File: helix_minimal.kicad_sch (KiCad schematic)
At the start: 15 parts, among them J1 USB-C, J2 WIZ850io J1, J3 WIZ850io J2, J4 3V3 microSD SPI breakout, J5 SWD, U1 STM32C071FBP6, U2 AP2112K-3.3

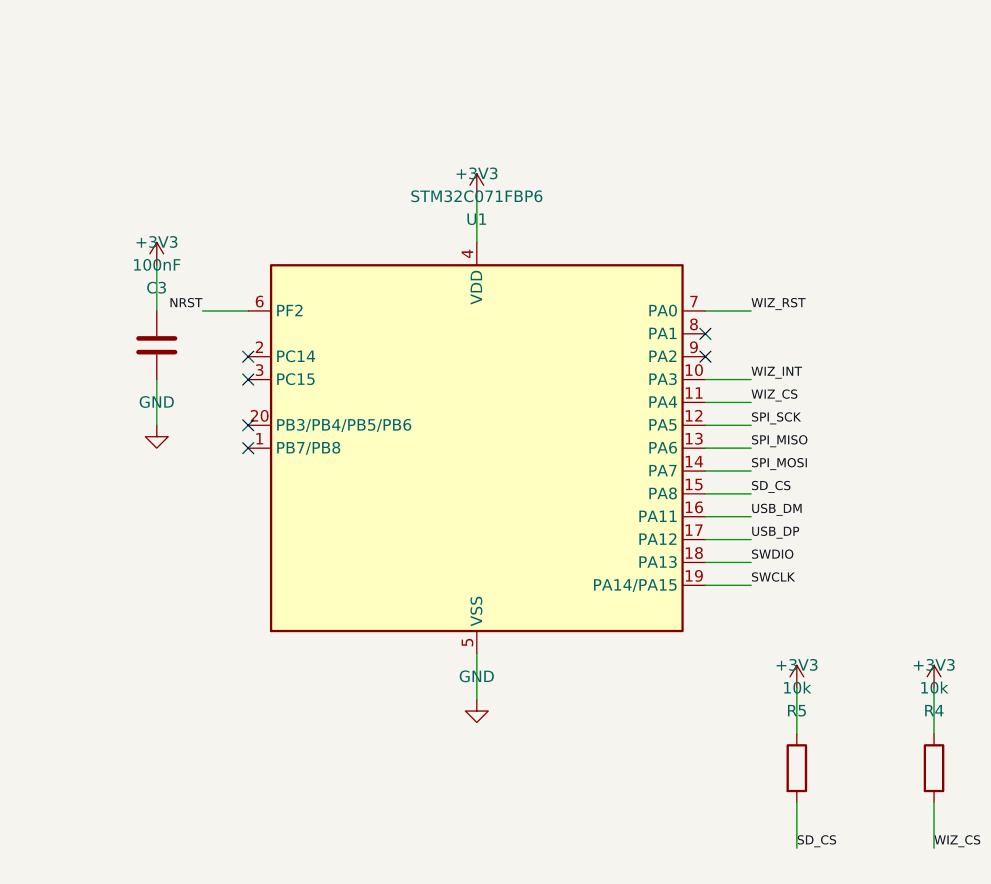
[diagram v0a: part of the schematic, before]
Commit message: Align STM32 connections with edited symbol
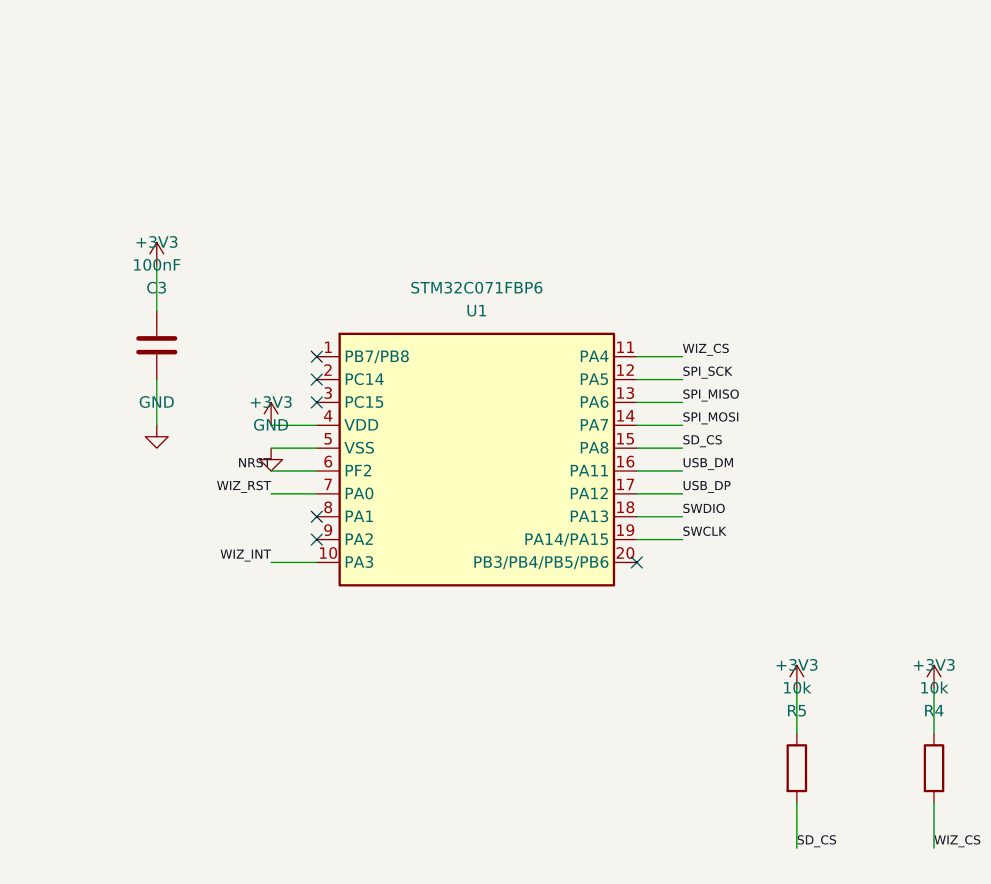
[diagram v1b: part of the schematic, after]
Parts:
- U1: symbol MCU_ST_STM32C0:STM32C071FBPx -> Helix:STM32C071FBPx
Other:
- moved on the sheet: U1

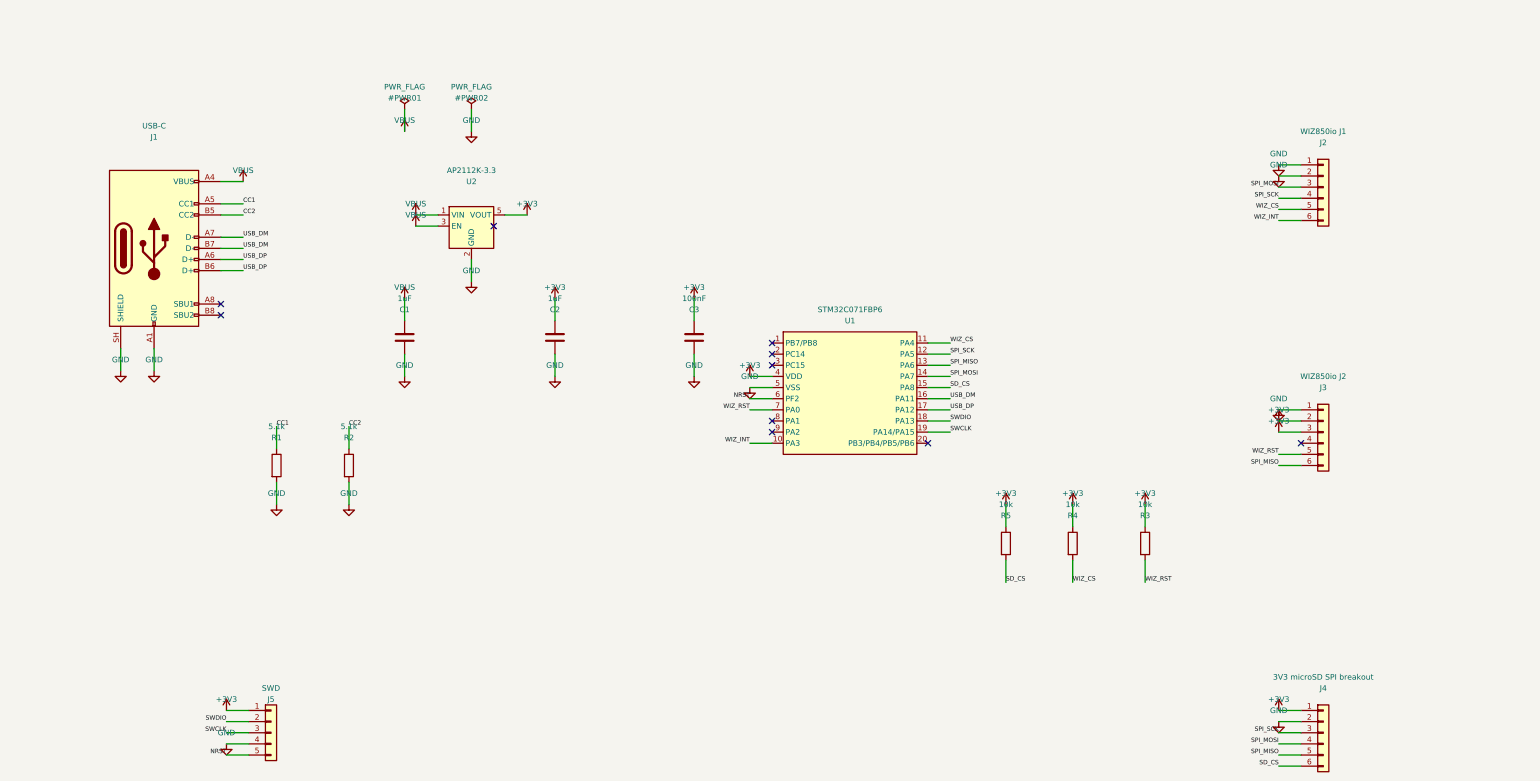
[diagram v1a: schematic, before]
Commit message: Restore KiCad edits and guard schematic generation
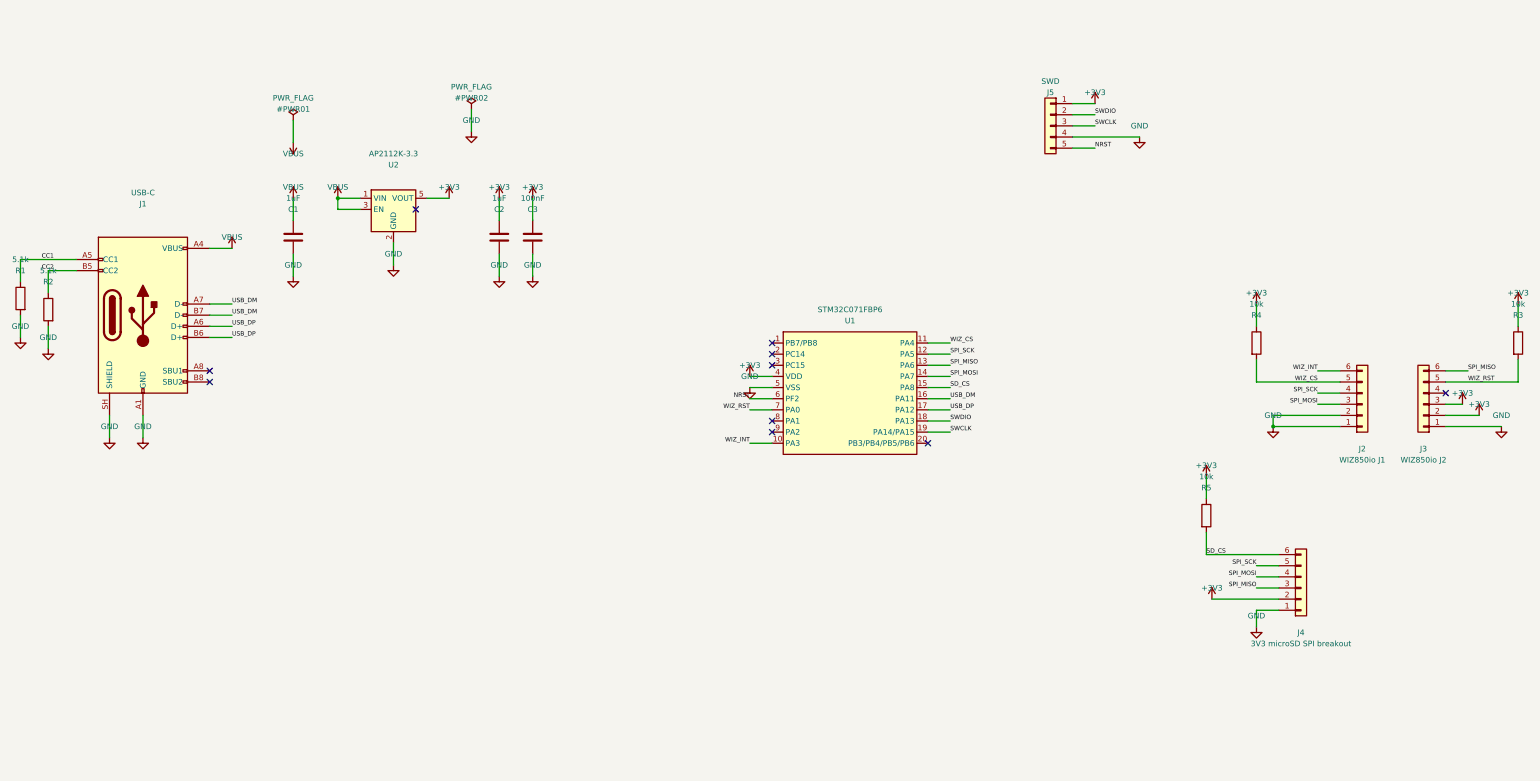
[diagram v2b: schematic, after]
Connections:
- net +3V3: now also J4.2 (Pin_2); no longer J4.1 (Pin_1)
- net GND: now also J4.1 (Pin_1); no longer J4.2 (Pin_2)
- net SPI_MISO: now also J4.3 (Pin_3); no longer J4.5 (Pin_5)
- net SPI_SCK: now also J4.5 (Pin_5); no longer J4.3 (Pin_3)
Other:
- moved on the sheet: C1, C2, C3, J1, J2, J3, J4, J5, R1, R2, R3, R4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

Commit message: Use WIZ850io module symbol and sourced footprint
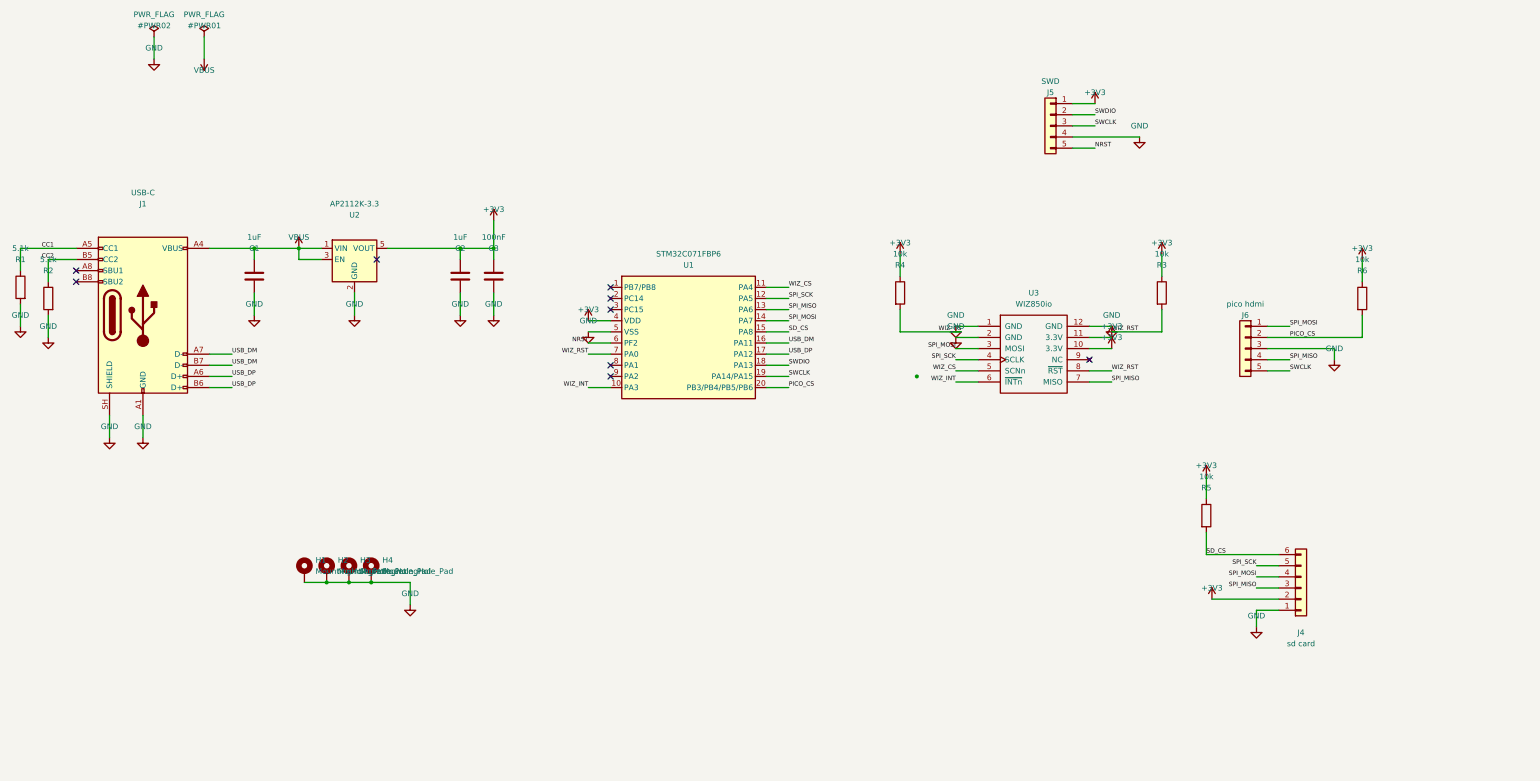
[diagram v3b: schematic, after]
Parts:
- removed J2: WIZ850io J1, Connector_PinSocket_2.54mm:PinSocket_1x06_P2.54mm_Vertical, symbol Connector_Generic:Conn_01x06
- removed J3: WIZ850io J2, Connector_PinSocket_2.54mm:PinSocket_1x06_P2.54mm_Vertical, symbol Connector_Generic:Conn_01x06
- added H1, H2, H3, H4: MountingHole_Pad, MountingHole:MountingHole_2.5mm_Pad, symbol Mechanical:MountingHole_Pad
- added J6: pico hdmi, Connector_PinHeader_2.54mm:PinHeader_1x05_P2.54mm_Vertical, symbol Connector_Generic:Conn_01x05
- added R6: 10k, custom_parts:R_0805_2012Metric_Pad1.20x1.40mm_HandSolder, symbol Device:R
- added U3: WIZ850io, Helix:WIZ850io, symbol WIZ850io:WIZ850io
- C1, C2, C3: footprint Capacitor_SMD:C_0603_1608Metric -> custom_parts:R_0805_2012Metric_Pad1.20x1.40mm_HandSolder
- J4: value 3V3 microSD SPI breakout -> sd card
- R1, R2, R3, R4, R5: footprint Resistor_SMD:R_0603_1608Metric -> custom_parts:R_0805_2012Metric_Pad1.20x1.40mm_HandSolder
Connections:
- net +3V3: now also R6.1, U3.10 (3.3V), U3.11 (3.3V)
- net GND: now also H1.1, H2.1, H3.1, H4.1, J6.3 (Pin_3), U3.1 (GND), U3.12 (GND), U3.2 (GND)
- net SPI_MISO: now also J6.4 (Pin_4), U3.7 (MISO)
- net SPI_MOSI: now also J6.1 (Pin_1), U3.3 (MOSI)
- net SPI_SCK: now also U3.4 (SCLK)
- net SWCLK: now also J6.5 (Pin_5)
- net WIZ_CS: now also U3.5 (SCNn)
- net WIZ_INT: now also U3.6 (~{INTn})
- net WIZ_RST: now also U3.8 (~{RST})
- net PICO_CS: now reaches U1.20 (PB3/PB4/PB5/PB6)
- net PICO_CS: now also J6.2 (Pin_2), R6.2
- no-connect marks 10 -> 9
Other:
- moved on the sheet: C1, C2, C3, R1, R2, R3, R4, U1, U2

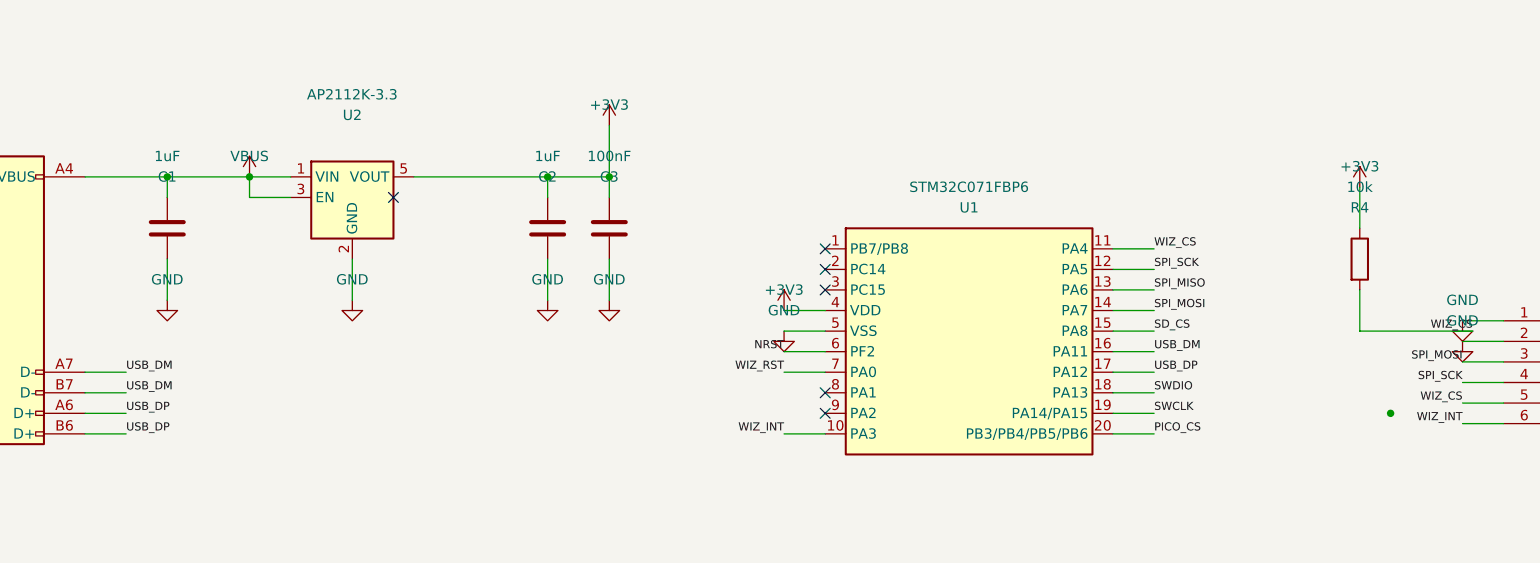
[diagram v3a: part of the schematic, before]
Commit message: Route around manual USB data pair and preserve schematic edits
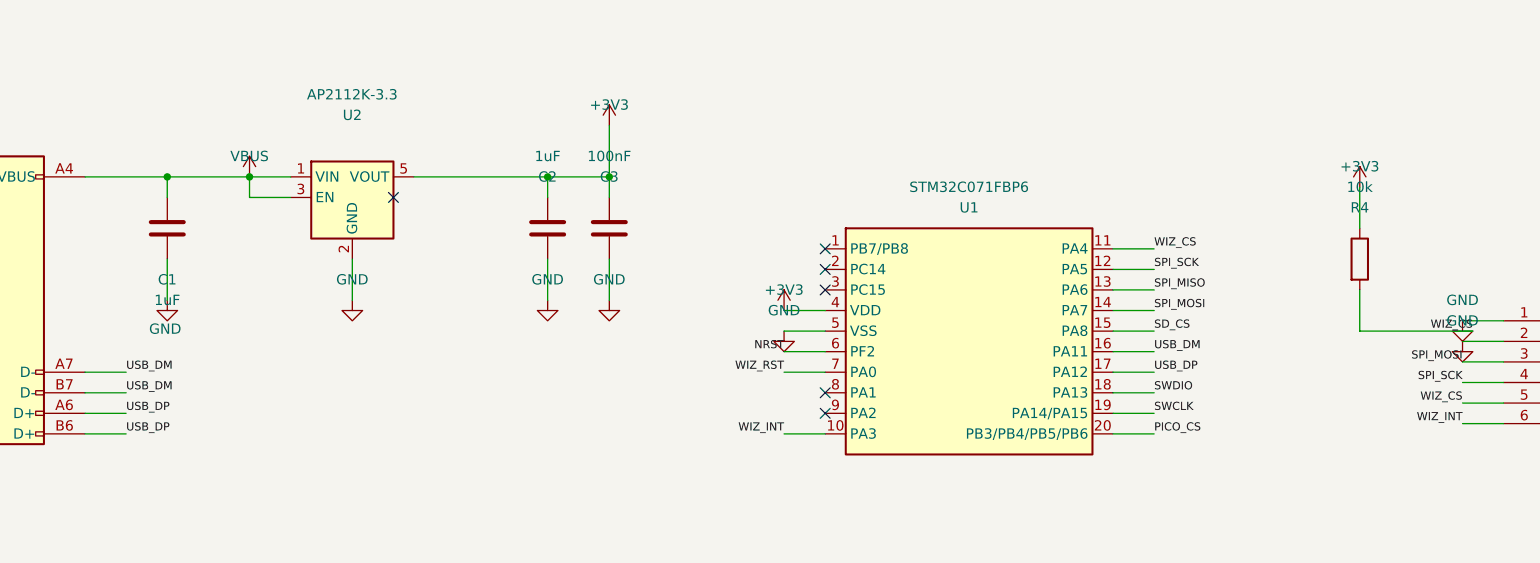
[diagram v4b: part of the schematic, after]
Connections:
- net GND: now also C1.1; no longer C1.2
- net VBUS: now also C1.2; no longer C1.1
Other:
- moved on the sheet: C1
